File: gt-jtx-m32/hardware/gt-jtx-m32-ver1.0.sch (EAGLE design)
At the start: 29 parts, among them IC1 MEGA32-P

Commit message: updated
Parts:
- removed AD0, AD1, AD2, AD3, AD4, AD5, AD6, AD7, D0, D1, D2, D3, D4, D5, D6, D7: (no value), pinhead:PINHD-1X3
- removed GNDC, TRIMS: (no value), pinhead:PINHD-1X8
- removed LED: (no value), led:LED5MM
- removed PWR: (no value), pinhead:PINHD-1X2
- removed R2: (no value), resistor:R-US_0204/2V
- added AIL, CH4, CH5, CH6, CH7, CH8, ELE, RUD, THR, X1, X2, X3, X4, X5, X6, X7: JST-XH-03-PIN-LONG-PAD, Rembrandt Electronics - JST XH Connectors v1-0:JST-XH-03-PIN-LONG-PAD
- added TRIM: TRIM, Rembrandt Electronics - JST XH Connectors v1-0:JST-XH-08-PIN-LONG-PAD
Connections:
- removed net +5V: AD0.2, AD1.2, AD2.2, AD3.2, AD4.2, AD5.2, AD6.2, AD7.2, D0.2, D1.2, D2.2, D3.2, D4.2, D5.2, D6.2, D7.2, IC1.AREF, IC1.AVCC, IC1.VCC, ISP.2, LED.A, PPM.2, PWR.1, R2.1, USART.4
- removed net GND: AD0.1, AD1.1, AD2.1, AD3.1, AD4.1, AD5.1, AD6.1, AD7.1, D0.1, D1.1, D2.1, D3.1, D4.1, D5.1, D6.1, D7.1, GNDC.1, GNDC.2, GNDC.3, GNDC.4, GNDC.5, GNDC.6, GNDC.7, GNDC.8, IC1.GND, IC1.GND@1, ISP.6, JP3.1, JP4.1, LED.C, PPM.3, PWR.2, USART.1
- removed net N$18: IC1.(TDI)PC5, TRIMS.3
- removed net N$19: IC1.(TDO)PC4, TRIMS.4
- removed net N$20: IC1.(TMS)PC3, TRIMS.5
- removed net N$21: IC1.(TCK)PC2, TRIMS.6
- removed net N$22: IC1.(SDA)PC1, TRIMS.7
- removed net N$23: IC1.(SCL)PC0, TRIMS.8
- new net N$34: IC1.GND, IC1.GND@1, ISP.6, JP3.1, JP4.1, PPM.3, USART.1, X1-1.S, X2-1.S, X3-1.S, X4-1.S, X5-1.S, X6-1.S, X7-1.S
- new net N$35: ELE-3.S, IC1.(ADC6)PA6
- new net N$36: IC1.AREF, IC1.AVCC, IC1.VCC, ISP.2, PPM.2, USART.4, X1-2.S, X2-2.S, X3-2.S, X4-2.S, X5-2.S, X6-2.S, X7-2.S
- new net N$37: IC1.(ADC5)PA5, THR-3.S
- new net N$38: IC1.(ADC4)PA4, RUD-3.S
- new net N$39: CH4-3.S, IC1.(ADC3)PA3
- new net N$40: CH5-3.S, IC1.(ADC2)PA2
- new net N$41: CH7-3.S, IC1.(ADC0)PA0
- net N$1: now also AIL-3.S, IC1.(ADC7)PA7; no longer AD7.3, IC1.(ADC0)PA0
- net N$10: now also IC1.(TMS)PC3, TRIM-5.S; no longer AD2.3, IC1.(ADC5)PA5
- net N$11: now also IC1.(TCK)PC2, TRIM-6.S; no longer AD1.3, IC1.(ADC6)PA6
- net N$16: now also IC1.(SDA)PC1, TRIM-7.S; no longer IC1.(TOSC1)PC6, TRIMS.2
- net N$17: now also IC1.(SCL)PC0, TRIM-8.S; no longer AD0.3, IC1.(ADC7)PA7
- net N$2: now also CH6-3.S; no longer AD6.3
- net N$24: now also X5-3.S; no longer D3.3
- net N$25: now also X4-3.S; no longer D4.3
- net N$26: now also X3-3.S; no longer D5.3
- net N$27: now also X2-3.S; no longer D6.3
- net N$28: now also X1-3.S; no longer D7.3
- net N$29: now also X6-3.S; no longer D2.3
- net N$3: now also IC1.(TOSC2)PC7, TRIM-1.S; no longer AD5.3, IC1.(ADC2)PA2
- net N$30: now also X7-3.S; no longer D1.3
- net N$31: now also CH8-3.S; no longer D0.3
- net N$4: now also IC1.(TOSC1)PC6, TRIM-2.S; no longer AD4.3, IC1.(ADC3)PA3
- net N$7: now also IC1.(TDI)PC5, TRIM-3.S; no longer IC1.(TOSC2)PC7, TRIMS.1
- net N$8: now also IC1.(TDO)PC4, TRIM-4.S; no longer AD3.3, IC1.(ADC4)PA4
- net N$9: no longer R2.2
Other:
- moved on the sheet: JP1, JP2, JP3, JP4, PPM

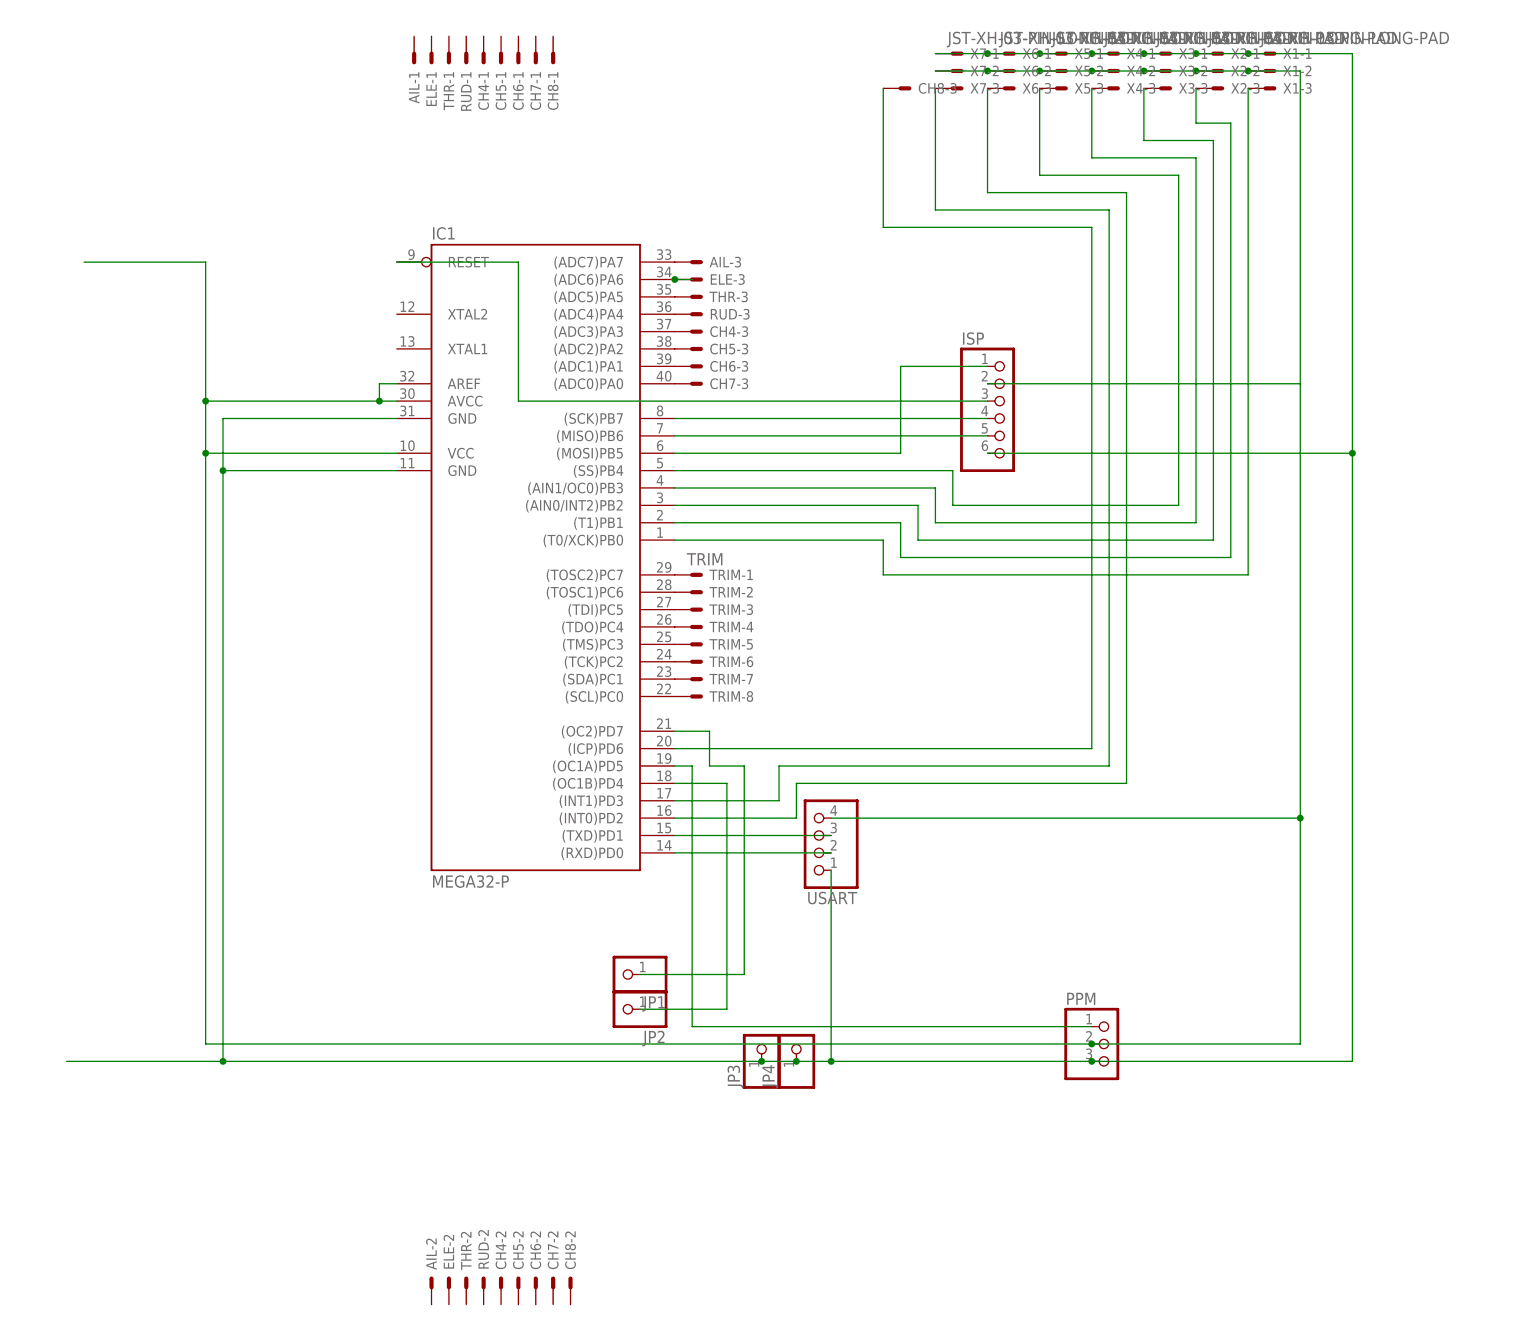
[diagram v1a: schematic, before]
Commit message: updated board design for new firmware mechanics with oled
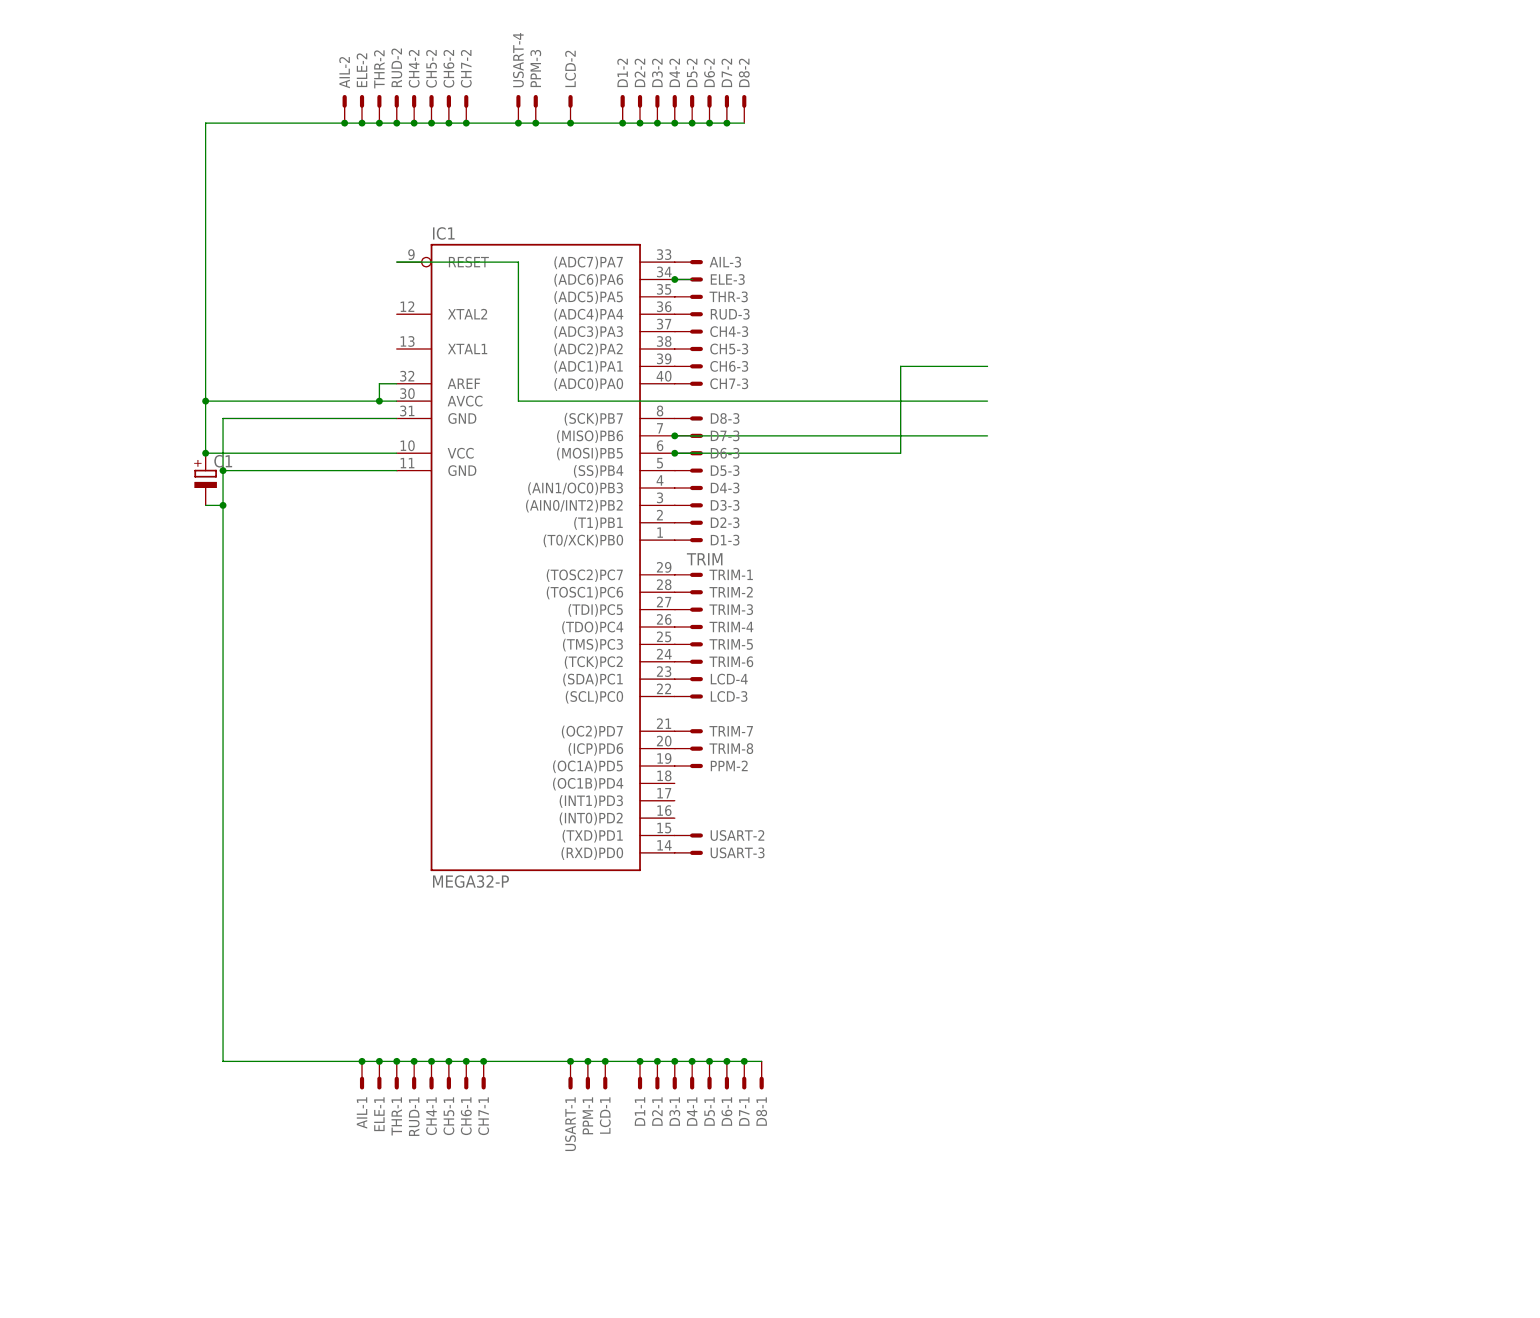
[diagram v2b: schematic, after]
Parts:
- removed CH8, X1, X2, X3, X4, X5, X6, X7: JST-XH-03-PIN-LONG-PAD, Rembrandt Electronics - JST XH Connectors v1-0:JST-XH-03-PIN-LONG-PAD
- removed ISP: (no value), pinhead:PINHD-1X6
- removed JP1, JP2, JP3, JP4: (no value), pinhead:PINHD-1X1
- added C1: (no value), rcl:CPOL-EUC
- added D1, D2, D3, D4, D5, D6, D7, D8: JST-XH-03-PIN-LONG-PAD, Rembrandt Electronics - JST XH Connectors v1-0:JST-XH-03-PIN-LONG-PAD
- added LCD: JST-XH-04-PIN-LONG-PAD, Rembrandt Electronics - JST XH Connectors v1-0:JST-XH-04-PIN-LONG-PAD
- PPM: value (none) -> JST-XH-03-PIN-LONG-PAD; device pinhead:PINHD-1X3 -> Rembrandt Electronics - JST XH Connectors v1-0:JST-XH-03-PIN-LONG-PAD
- USART: value (none) -> JST-XH-04-PIN-LONG-PAD; device pinhead:PINHD-1X4 -> Rembrandt Electronics - JST XH Connectors v1-0:JST-XH-04-PIN-LONG-PAD
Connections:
- removed net N$27: IC1.(T1)PB1, X2-3.S
- removed net N$28: IC1.(T0/XCK)PB0, X1-3.S
- removed net N$29: IC1.(INT0)PD2, X6-3.S
- removed net N$30: IC1.(INT1)PD3, X7-3.S
- removed net N$31: CH8-3.S, IC1.(ICP)PD6
- removed net N$32: IC1.(OC1B)PD4, JP2.1
- removed net N$33: IC1.(OC2)PD7, JP1.1
- removed net N$34: IC1.GND, IC1.GND@1, ISP.6, JP3.1, JP4.1, PPM.3, USART.1, X1-1.S, X2-1.S, X3-1.S, X4-1.S, X5-1.S, X6-1.S, X7-1.S
- removed net N$36: IC1.AREF, IC1.AVCC, IC1.VCC, ISP.2, PPM.2, USART.4, X1-2.S, X2-2.S, X3-2.S, X4-2.S, X5-2.S, X6-2.S, X7-2.S
- new net GND: AIL-1.S, C1.-, CH4-1.S, CH5-1.S, CH6-1.S, CH7-1.S, D1-1.S, D2-1.S, D3-1.S, D4-1.S, D5-1.S, D6-1.S, D7-1.S, D8-1.S, ELE-1.S, IC1.GND, IC1.GND@1, LCD-1.S, PPM-1.S, RUD-1.S, THR-1.S, USART-1.S
- new net N$18: IC1.(RXD)PD0, USART-3.S
- new net N$19: IC1.(SDA)PC1, LCD-4.S
- new net N$22: IC1.(SCL)PC0, LCD-3.S
- new net N$23: IC1.(OC1A)PD5, PPM-2.S
- new net VCC: AIL-2.S, C1.+, CH4-2.S, CH5-2.S, CH6-2.S, CH7-2.S, D1-2.S, D2-2.S, D3-2.S, D4-2.S, D5-2.S, D6-2.S, D7-2.S, D8-2.S, ELE-2.S, IC1.AREF, IC1.AVCC, IC1.VCC, LCD-2.S, PPM-3.S, RUD-2.S, THR-2.S, USART-4.S
- net N$12: now also D6-3.S; no longer ISP.1
- net N$13: now also D7-3.S; no longer ISP.5
- net N$14: now also D8-3.S; no longer ISP.4
- net N$15: now also D2-3.S, IC1.(T1)PB1; no longer IC1.(OC1A)PD5, PPM.1
- net N$16: now also IC1.(OC2)PD7; no longer IC1.(SDA)PC1
- net N$17: now also IC1.(ICP)PD6; no longer IC1.(SCL)PC0
- net N$24: now also D3-3.S, IC1.(AIN0/INT2)PB2; no longer IC1.(SS)PB4, X5-3.S
- net N$25: now also D4-3.S; no longer X4-3.S
- net N$26: now also D5-3.S, IC1.(SS)PB4; no longer IC1.(AIN0/INT2)PB2, X3-3.S
- net N$5: now also D1-3.S, IC1.(T0/XCK)PB0; no longer IC1.(RXD)PD0, USART.2
- net N$6: now also USART-2.S; no longer USART.3
- net N$9: no longer ISP.3
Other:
- moved on the sheet: AIL-1, AIL-2, CH4-1, CH4-2, CH5-1, CH5-2, CH6-1, CH6-2, CH7-1, CH7-2, ELE-1, ELE-2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

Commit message: updated board with led and isp header updated code with newer structure of using rx/tx
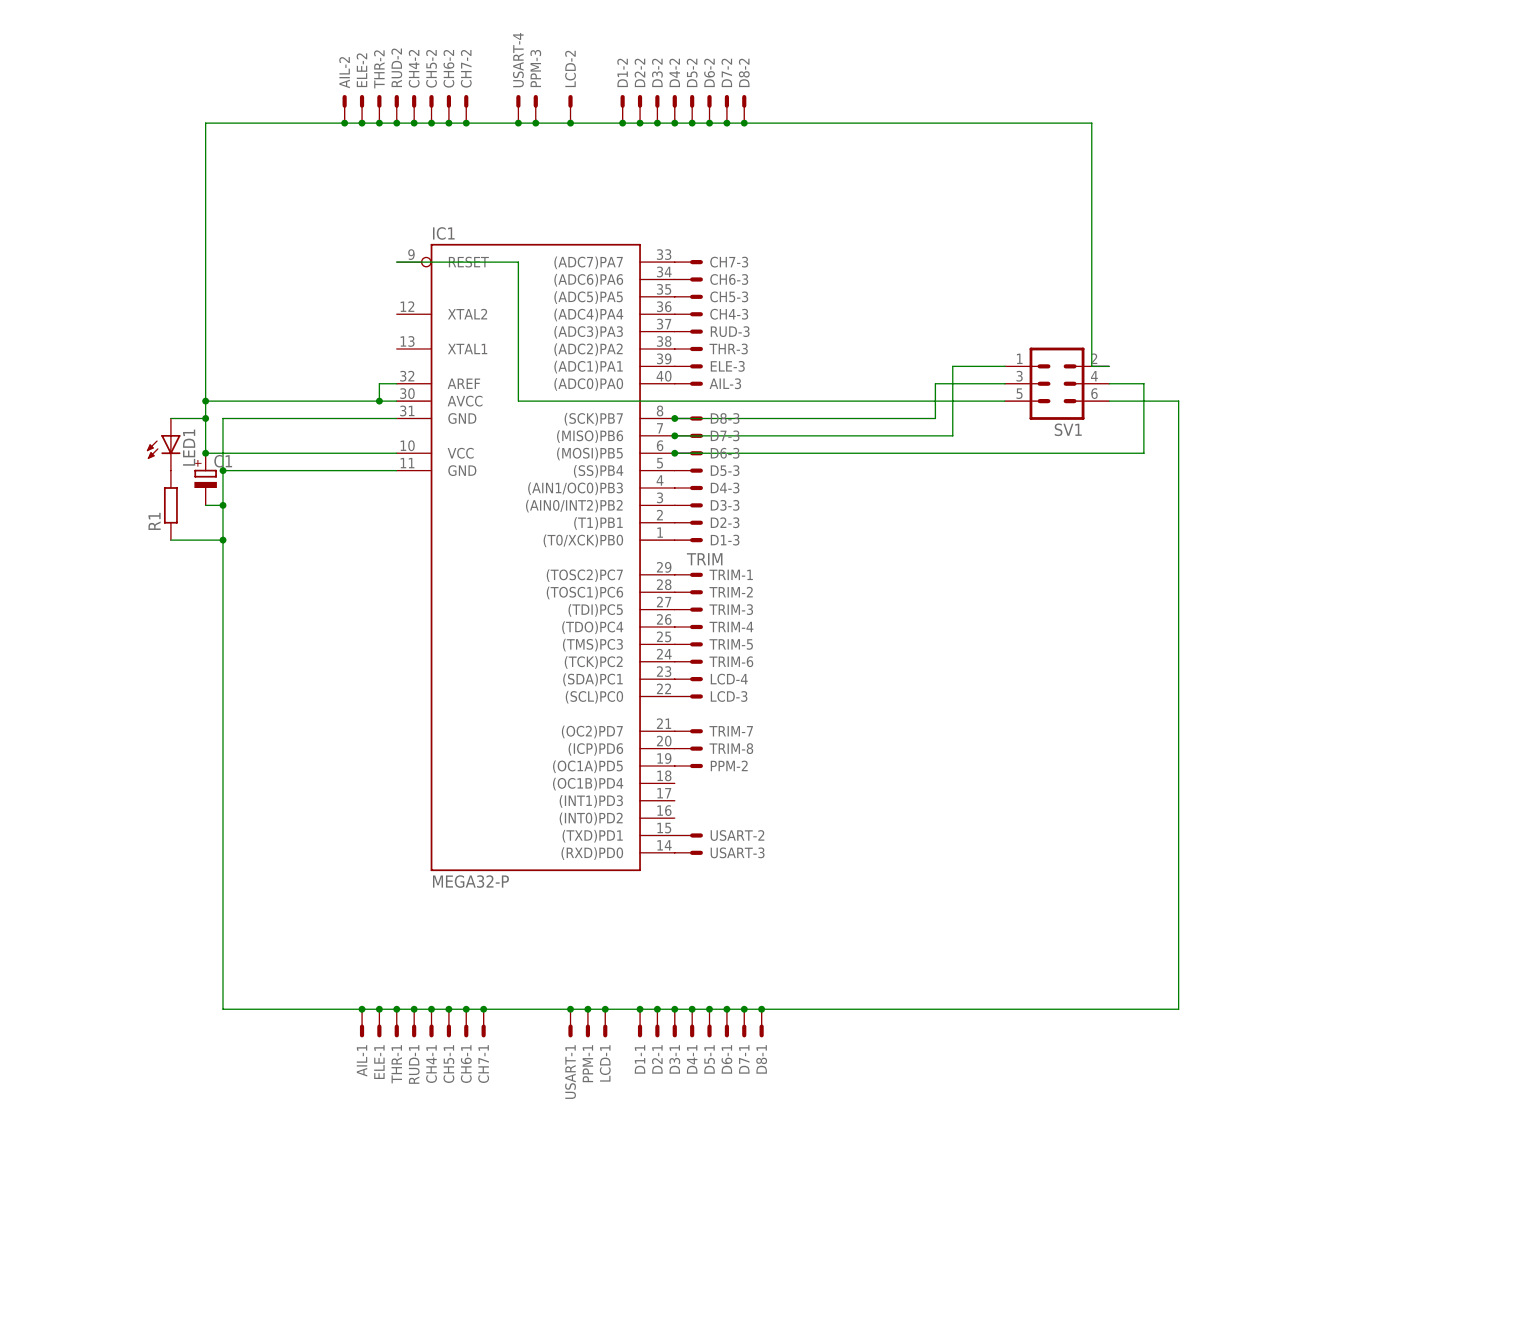
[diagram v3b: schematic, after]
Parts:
- added LED1: (no value), led:LED5MM
- added R1: (no value), eagle-ltspice:R0204/7
- added SV1: (no value), con-lstb:MA03-2
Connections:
- removed net N$35: ELE-3.S, IC1.(ADC6)PA6
- removed net N$37: IC1.(ADC5)PA5, THR-3.S
- removed net N$38: IC1.(ADC4)PA4, RUD-3.S
- removed net N$39: CH4-3.S, IC1.(ADC3)PA3
- removed net N$40: CH5-3.S, IC1.(ADC2)PA2
- removed net N$41: CH7-3.S, IC1.(ADC0)PA0
- new net N$20: CH7-3.S, IC1.(ADC7)PA7
- new net N$21: CH4-3.S, IC1.(ADC4)PA4
- new net N$27: IC1.(ADC3)PA3, RUD-3.S
- new net N$28: IC1.(ADC2)PA2, THR-3.S
- new net N$29: ELE-3.S, IC1.(ADC1)PA1
- new net N$30: AIL-3.S, IC1.(ADC0)PA0
- new net N$32: LED1.C, R1.2
- net GND: now also R1.1, SV1.6
- net N$1: now also CH5-3.S, IC1.(ADC5)PA5; no longer AIL-3.S, IC1.(ADC7)PA7
- net N$12: now also SV1.4
- net N$13: now also SV1.1
- net N$14: now also SV1.3
- net N$2: now also IC1.(ADC6)PA6; no longer IC1.(ADC1)PA1
- net N$9: now also SV1.5
- net VCC: now also LED1.A, SV1.2
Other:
- moved on the sheet: AIL-1, AIL-3, CH4-1, CH4-3, CH5-1, CH5-3, CH6-1, CH6-3, CH7-1, CH7-3, D1-1, D2-1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
